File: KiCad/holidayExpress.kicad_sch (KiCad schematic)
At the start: 18 parts, among them J1 Screw_Terminal_01x02, J2 Screw_Terminal_01x04, SW1 SW_Push, U1 ESP32-PICO-MINI-02, U2 DRV8833PW, U3 MPM3610GQV-P

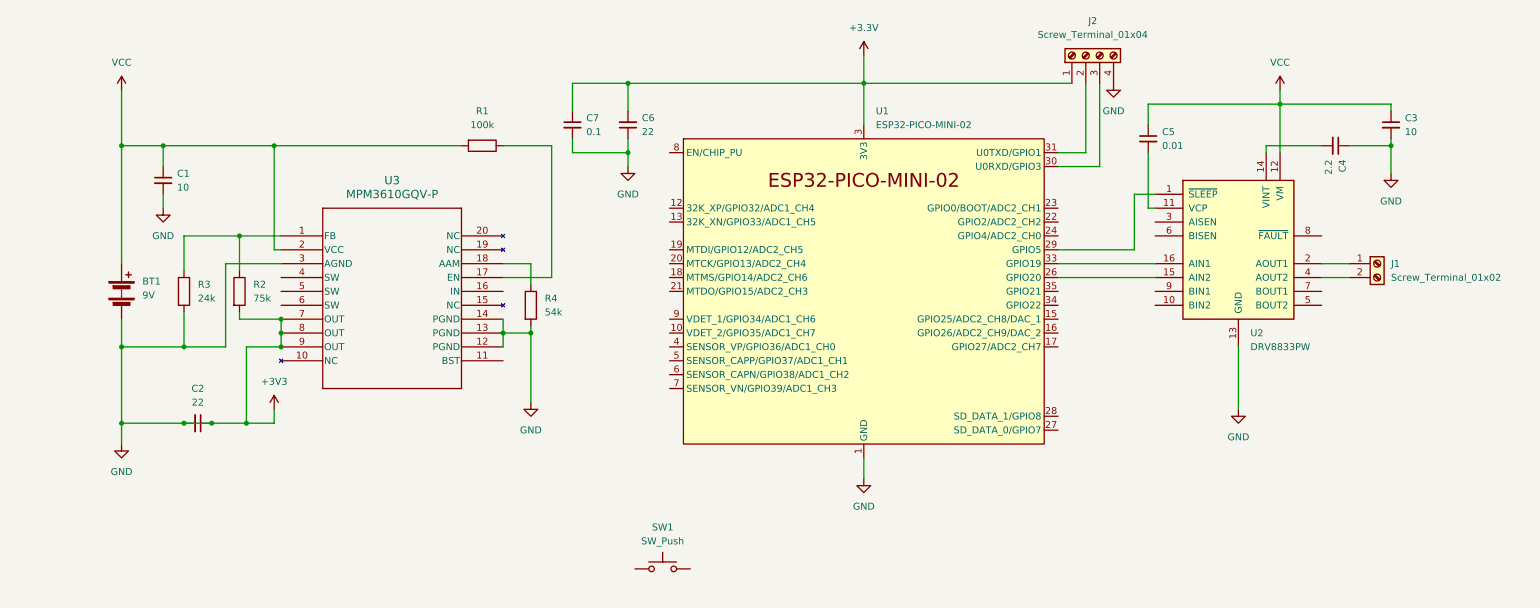
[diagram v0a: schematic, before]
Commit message: add boot and reset buttons
Finish initial prototype schematic with reset and boot buttons for getting into flashing boot mode.
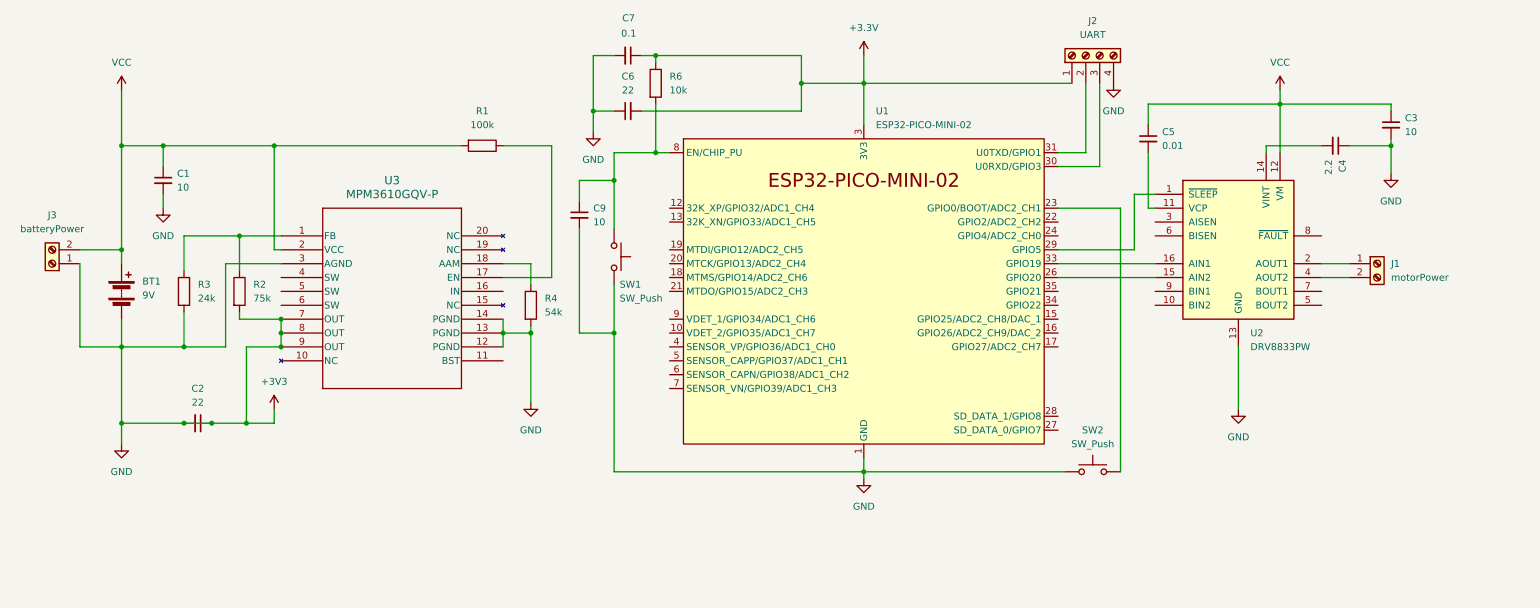
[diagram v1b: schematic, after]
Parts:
- added C9: 10, symbol Device:C_Small
- added J3: batteryPower, symbol Connector:Screw_Terminal_01x02
- added R6: 10k, symbol Device:R
- added SW2: SW_Push, symbol Switch:SW_Push
- J1: value Screw_Terminal_01x02 -> motorPower
- J2: value Screw_Terminal_01x04 -> UART
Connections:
- net +3.3V: now also R6.1
- net +3V3: now also SW1.2, C9.2, J3.1 (Pin_1), SW2.1
- net VCC: now also J3.2 (Pin_2)
- net at U1.23 (GPIO0/BOOT/ADC2_CH1): now also SW2.2
- net at U1.8 (EN/CHIP_PU): now also SW1.1, C9.1, R6.2
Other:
- moved on the sheet: C6, C7, SW1

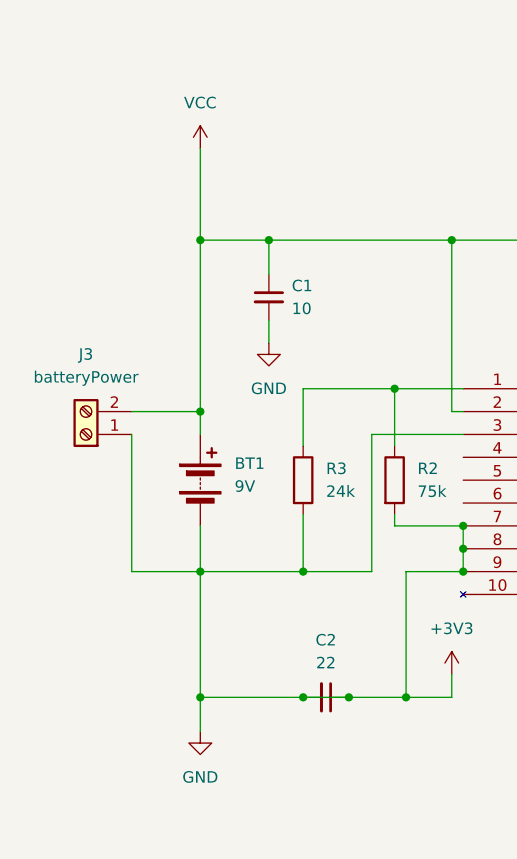
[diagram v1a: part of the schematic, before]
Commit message: add initial footprint selections
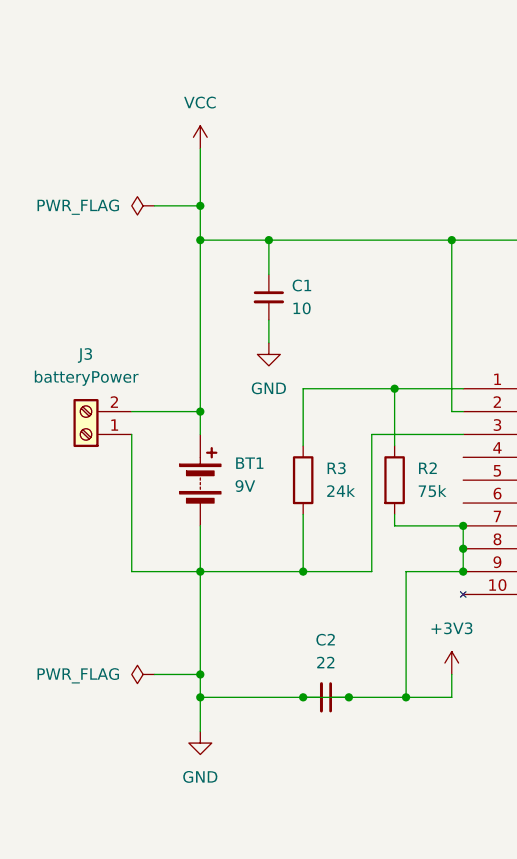
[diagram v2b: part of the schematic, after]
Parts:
- C1, C2, C3, C4, C5, C6, C7, C9, J1, J2: footprint (none) -> Capacitor_SMD:C_0402_1005Metric
- R1, R2, R3, R4, R6: footprint (none) -> Resistor_SMD:R_0402_1005Metric
- U2: footprint Package_SO:TSSOP-16_4.4x5mm_P0.65mm -> Package_DFN_QFN:Texas_RTY_WQFN-16-1EP_4x4mm_P0.65mm_EP2.1x2.1mm_ThermalVias
- U3: footprint QFN3p0x5p0x1p6_MPM3610_MNP -> footprints:QFN3p0x5p0x1p6_MPM3610_MNP
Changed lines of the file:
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@@
 	)
 	(junction
+		(at 31.75 34.29)
+		(diameter 0)
+		(color 0 0 0 0)
+	)
+	(junction
 		(at 31.75 74.93)
 		(diameter 0)
@@
 	)
 	(junction
+		(at 31.75 86.36)
+		(diameter 0)
+		(color 0 0 0 0)
+	)
+	(junction
 		(at 31.75 57.15)
 		(diameter 0)
@@
 	(wire
 		(pts
-			(xy 31.75 27.94) (xy 31.75 38.1)
+			(xy 31.75 27.94) (xy 31.75 34.29)
+		)
+		(stroke
+			(width 0)
+			(type default)
+		)
+	)
+	(wire
+		(pts
+			(xy 26.67 86.36) (xy 31.75 86.36)
 		)
 		(stroke
@@
 	(wire
 		(pts
-			(xy 31.75 74.93) (xy 31.75 88.9)
+			(xy 31.75 74.93) (xy 31.75 86.36)
 		)
 		(stroke
@@
 	(wire
 		(pts
+			(xy 31.75 34.29) (xy 31.75 38.1)
+		)
+		(stroke
+			(width 0)
+			(type default)
+		)
+	)
+	(wire
+		(pts
 			(xy 251.46 62.23) (xy 256.54 62.23)
 		)
@@
 	(wire
 		(pts
+			(xy 31.75 86.36) (xy 31.75 88.9)
+		)
+		(stroke
+			(width 0)
+			(type default)
+		)
+	)
+	(wire
+		(pts
 			(xy 101.6 72.39) (xy 101.6 74.93)
 		)
@@
 	(wire
 		(pts
+			(xy 26.67 34.29) (xy 31.75 34.29)
+		)
+		(stroke
+			(width 0)
+			(type default)
+		)
+	)
+	(wire
+		(pts
 			(xy 101.6 59.69) (xy 106.68 59.69)
 		)
@@
 			)
 		)
-		(property "Footprint" ""
+		(property "Footprint" "Capacitor_SMD:C_0402_1005Metric"
 			(at 39.37 44.45 0)
 			(effects
@@
 			)
 		)
-		(property "Footprint" ""
+		(property "Footprint" "Capacitor_SMD:C_0402_1005Metric"
 			(at 254 38.1 0)
 			(effects
@@
 			)
 		)
-		(property "Footprint" ""
+		(property "Footprint" "Capacitor_SMD:C_0402_1005Metric"
 			(at 124.46 21.59 0)
 			(effects
@@
 			)
 		)
-		(property "Footprint" ""
+		(property "Footprint" "Capacitor_SMD:C_0402_1005Metric"
 			(at 264.16 34.29 0)
 			(effects
@@
 			)
 		)
-		(property "Footprint" ""
+		(property "Footprint" "Resistor_SMD:R_0402_1005Metric"
 			(at 104.902 67.31 90)
 			(effects
@@
 			)
 		)
-		(property "Footprint" ""
+		(property "Footprint" "Capacitor_SMD:C_0402_1005Metric"
 			(at 261.62 59.69 0)
 			(effects
@@
 			)
 		)
-		(property "Footprint" ""
+		(property "Footprint" "Capacitor_SMD:C_0402_1005Metric"
 			(at 115.57 50.8 0)
 			(effects
@@
 			)
 		)
-		(property "Footprint" ""
+		(property "Footprint" "Resistor_SMD:R_0402_1005Metric"
 			(at 97.79 36.322 90)
 			(effects
@@
 			)
 		)
-		(property "Footprint" ""
+		(property "Footprint" "Capacitor_SMD:C_0402_1005Metric"
 			(at 124.46 31.75 0)
 			(effects
@@
 			)
 		)
-		(property "Footprint" ""
+		(property "Footprint" "Capacitor_SMD:C_0402_1005Metric"
 			(at 45.72 88.9 0)
 			(effects
@@
 	)
 	(symbol
+		(lib_id "power:PWR_FLAG")
+		(at 26.67 86.36 90)
+		(unit 1)
+		(exclude_from_sim no)
+		(in_bom yes)
+		(on_board yes)
+		(dnp no)
+		(fields_autoplaced yes)
+		(property "Reference" "#FLG02"
+			(at 24.765 86.36 0)
+			(effects
+				(font
+					(size 1.27 1.27)
+				)
+				(hide yes)
+			)
+		)
+		(property "Value" "PWR_FLAG"
+			(at 22.86 86.3599 90)
+			(effects
+				(font
+					(size 1.27 1.27)
+				)
+				(justify left)
+			)
+		)
+		(property "Footprint" ""
+			(at 26.67 86.36 0)
+			(effects
+				(font
+					(size 1.27 1.27)
+				)
+				(hide yes)
+			)
+		)
+		(property "Datasheet" "~"
+			(at 26.67 86.36 0)
+			(effects
+				(font
+					(size 1.27 1.27)
+				)
+				(hide yes)
+			)
+		)
+		(property "Description" "Special symbol for telling ERC where power comes from"
+			(at 26.67 86.36 0)
+			(effects
+				(font
+					(size 1.27 1.27)
+				)
+				(hide yes)
+			)
+		)
+		(pin "1"
+		)
+		(instances
+			(project ""
+				(path "/c3dabb1a-9ea8-4f8f-9e0b-7c4553d29435"
+					(reference "#FLG02")
+					(unit 1)
+				)
+			)
+		)
+	)
+	(symbol
 		(lib_id "Connector:Screw_Terminal_01x02")
 		(at 19.05 59.69 180)
@@
 			)
 		)
-		(property "Footprint" ""
+		(property "Footprint" "Resistor_SMD:R_0402_1005Metric"
 			(at 127.762 26.67 90)
 			(effects
@@
 			)
 		)
-		(property "Footprint" ""
+		(property "Footprint" "Capacitor_SMD:C_0402_1005Metric"
 			(at 208.28 21.59 0)
 			(effects
@@
 			)
 		)
-		(property "Footprint" ""
+		(property "Footprint" "Capacitor_SMD:C_0402_1005Metric"
 			(at 219.71 36.83 0)
 			(effects
@@
 		(exclude_from_sim no)
 		(in_bom yes)
-		(on_board yes)
+		(on_board no)
 		(dnp no)
 		(fields_autoplaced yes)
@@
 			)
 		)
-		(property "Footprint" ""
+		(property "Footprint" "Resistor_SMD:R_0402_1005Metric"
 			(at 41.402 64.77 90)
 			(effects
@@
 			)
 		)
-		(property "Footprint" "Package_SO:TSSOP-16_4.4x5mm_P0.65mm"
+		(property "Footprint" "Package_DFN_QFN:Texas_RTY_WQFN-16-1EP_4x4mm_P0.65mm_EP2.1x2.1mm_ThermalVias"
 			(at 241.3 74.93 0)
 			(effects
@@
 			)
 		)
-		(property "Footprint" "QFN3p0x5p0x1p6_MPM3610_MNP"
+		(property "Footprint" "footprints:QFN3p0x5p0x1p6_MPM3610_MNP"
 			(at 60.96 54.61 0)
 			(effects
@@
 	)
 	(symbol
+		(lib_id "power:PWR_FLAG")
+		(at 26.67 34.29 90)
+		(unit 1)
+		(exclude_from_sim no)
+		(in_bom yes)
+		(on_board yes)
+		(dnp no)
+		(fields_autoplaced yes)
+		(property "Reference" "#FLG01"
+			(at 24.765 34.29 0)
+			(effects
+				(font
+					(size 1.27 1.27)
+				)
+				(hide yes)
+			)
+		)
+		(property "Value" "PWR_FLAG"
+			(at 22.86 34.2899 90)
+			(effects
+				(font
+					(size 1.27 1.27)
+				)
+				(justify left)
+			)
+		)
+		(property "Footprint" ""
+			(at 26.67 34.29 0)
+			(effects
+				(font
+					(size 1.27 1.27)
+				)
+				(hide yes)
+			)
+		)
+		(property "Datasheet" "~"
+			(at 26.67 34.29 0)
+			(effects
+				(font
+					(size 1.27 1.27)
+				)
+				(hide yes)
+			)
+		)
+		(property "Description" "Special symbol for telling ERC where power comes from"
+			(at 26.67 34.29 0)
+			(effects
+				(font
+					(size 1.27 1.27)
+				)
+				(hide yes)
+			)
+		)
+		(pin "1"
+		)
+		(instances
+			(project ""
+				(path "/c3dabb1a-9ea8-4f8f-9e0b-7c4553d29435"
+					(reference "#FLG01")
+					(unit 1)
+				)
+			)
+		)
+	)
+	(symbol
 		(lib_id "Device:R")
 		(at 53.34 64.77 0)
@@
 			)
 		)
-		(property "Footprint" ""
+		(property "Footprint" "Resistor_SMD:R_0402_1005Metric"
 			(at 51.562 64.77 90)
 			(effects

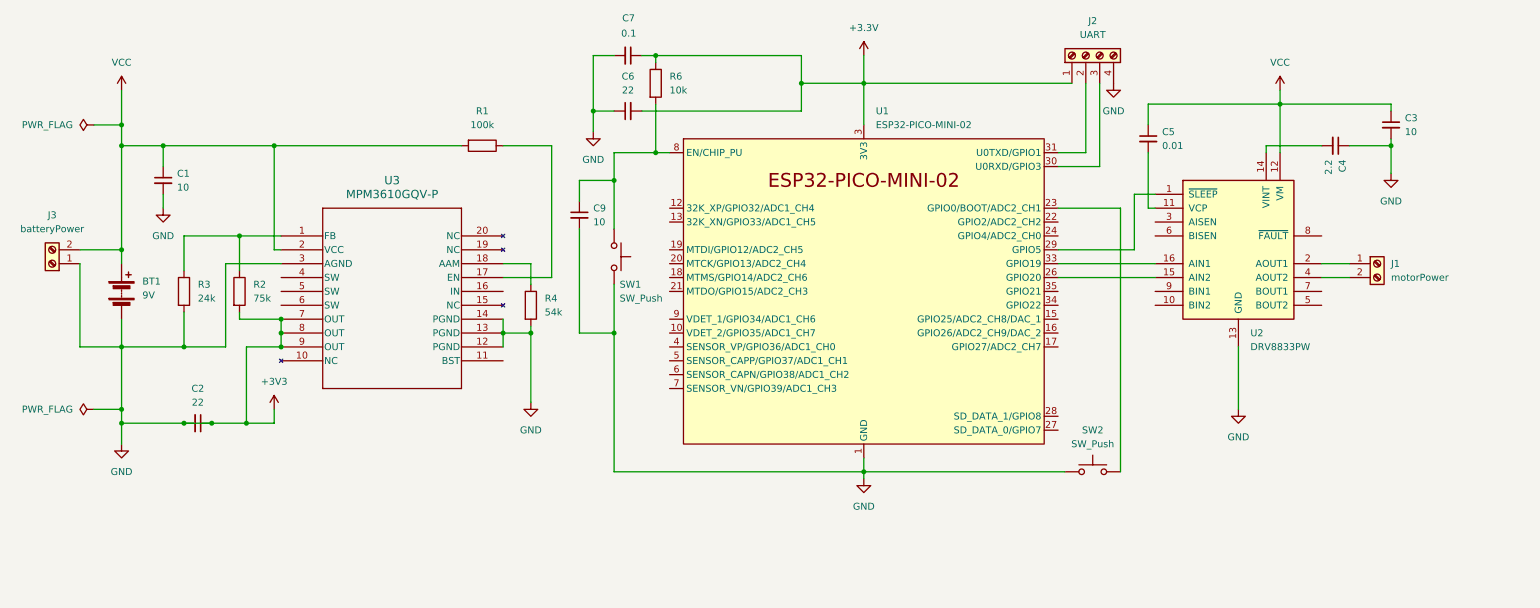
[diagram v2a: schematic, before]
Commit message: add SDM LED and change to pin headers
Add a power indicator LED. Change screw terminals to standard pin headers. Add project library for SMD LED symbol and footprint.

Create initial PCB layout.
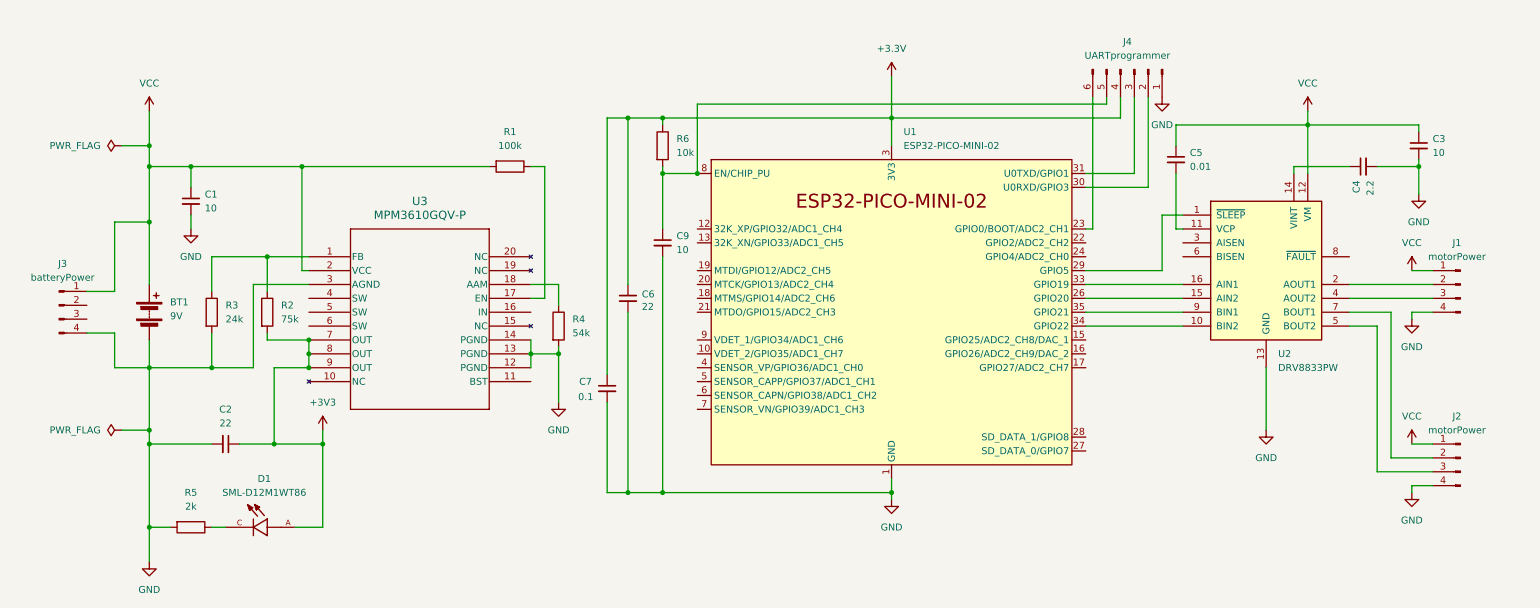
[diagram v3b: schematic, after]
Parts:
- removed J1: motorPower, Capacitor_SMD:C_0402_1005Metric, symbol Connector:Screw_Terminal_01x02
- removed J2: UART, Capacitor_SMD:C_0402_1005Metric, symbol Connector:Screw_Terminal_01x04
- removed J3: batteryPower, symbol Connector:Screw_Terminal_01x02
- removed SW1, SW2: SW_Push, symbol Switch:SW_Push
- added D1: SML-D12M1WT86, footprintDownloads:LED_SML-D12M1WT86, symbol symbolDownloads:SML-D12M1WT86
- added J1, J2: motorPower, Connector_PinHeader_2.54mm:PinHeader_1x04_P2.54mm_Horizontal, symbol Connector:Conn_01x04_Pin
- added J3: batteryPower, Connector_PinHeader_2.54mm:PinHeader_1x04_P2.54mm_Horizontal, symbol Connector:Conn_01x04_Pin
- added J4: UARTprogrammer, Connector_PinHeader_2.54mm:PinHeader_1x06_P2.54mm_Horizontal, symbol Connector:Conn_01x06_Pin
- added R5: 2k, Resistor_SMD:R_0402_1005Metric, symbol Device:R
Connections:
- net +3.3V: now also C6.1, J4.4 (Pin_4); no longer C6.2
- net +3V3: now also D1.A; no longer BT1.2 (-), C1.2, C2.2, C3.2, C4.1, C6.1, C7.2, C9.2, R3.2, R4.2, U1.1 (GND), U1.11 (GND), U1.14 (GND), U1.2 (GND), U1.36 (GND), U1.37 (GND), U1.38 (GND), U1.39 (GND), U1.40 (GND), U1.41 (GND), U1.42 (GND), U1.43 (GND), U1.44 (GND), U1.45 (GND), U1.46 (GND), U1.47 (GND), U1.48 (GND), U1.49 (GND), U1.50 (GND), U1.51 (GND), U1.52 (GND), U1.53 (GND), U2.13 (GND), U3.12 (PGND), U3.13 (PGND), U3.14 (PGND), U3.3 (AGND)
- net VCC: now also J1.1 (Pin_1), J2.1 (Pin_1), J3.1 (Pin_1)
- net at U2.14 (VINT): now also C4.1; no longer C4.2
- net at U1.23 (GPIO0/BOOT/ADC2_CH1): now also J4.6 (Pin_6)
- net at U2.2 (AOUT1): now also J1.2 (Pin_2)
- net at U2.4 (AOUT2): now also J1.3 (Pin_3)
- net at C9.1, R6.2, U1.8 (EN/CHIP_PU): now also J4.5 (Pin_5)
- net at U1.31 (U0TXD/GPIO1): now also J4.3 (Pin_3)
- net at U1.30 (U0RXD/GPIO3): now also J4.2 (Pin_2)
- net at U1.34 (GPIO22): now also U2.10 (BIN2)
- net at U1.35 (GPIO21): now also U2.9 (BIN1)
- net at U2.5 (BOUT2): now also J2.3 (Pin_3)
- net at U2.7 (BOUT1): now also J2.2 (Pin_2)
- new net: D1.C, R5.1
- new net GND: BT1.2 (-), C1.2, C2.2, C3.2, C4.2, C6.2, C7.2, C9.2, J1.4 (Pin_4), J2.4 (Pin_4), J3.4 (Pin_4), J4.1 (Pin_1), R3.2, R4.2, R5.2, U1.1 (GND), U1.11 (GND), U1.14 (GND), U1.2 (GND), U1.36 (GND), U1.37 (GND), U1.38 (GND), U1.39 (GND), U1.40 (GND), U1.41 (GND), U1.42 (GND), U1.43 (GND), U1.44 (GND), U1.45 (GND), U1.46 (GND), U1.47 (GND), U1.48 (GND), U1.49 (GND), U1.50 (GND), U1.51 (GND), U1.52 (GND), U1.53 (GND), U2.13 (GND), U3.12 (PGND), U3.13 (PGND), U3.14 (PGND), U3.3 (AGND)
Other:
- title: holidayExpress_Circuit -> holidayExpress_schematic
- moved on the sheet: BT1, C1, C2, C3, C4, C5, C6, C7, C9, R1, R2, R3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
